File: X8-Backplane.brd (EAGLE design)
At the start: 122.1 x 106.6 mm, 14 parts, among them U1 LM2678

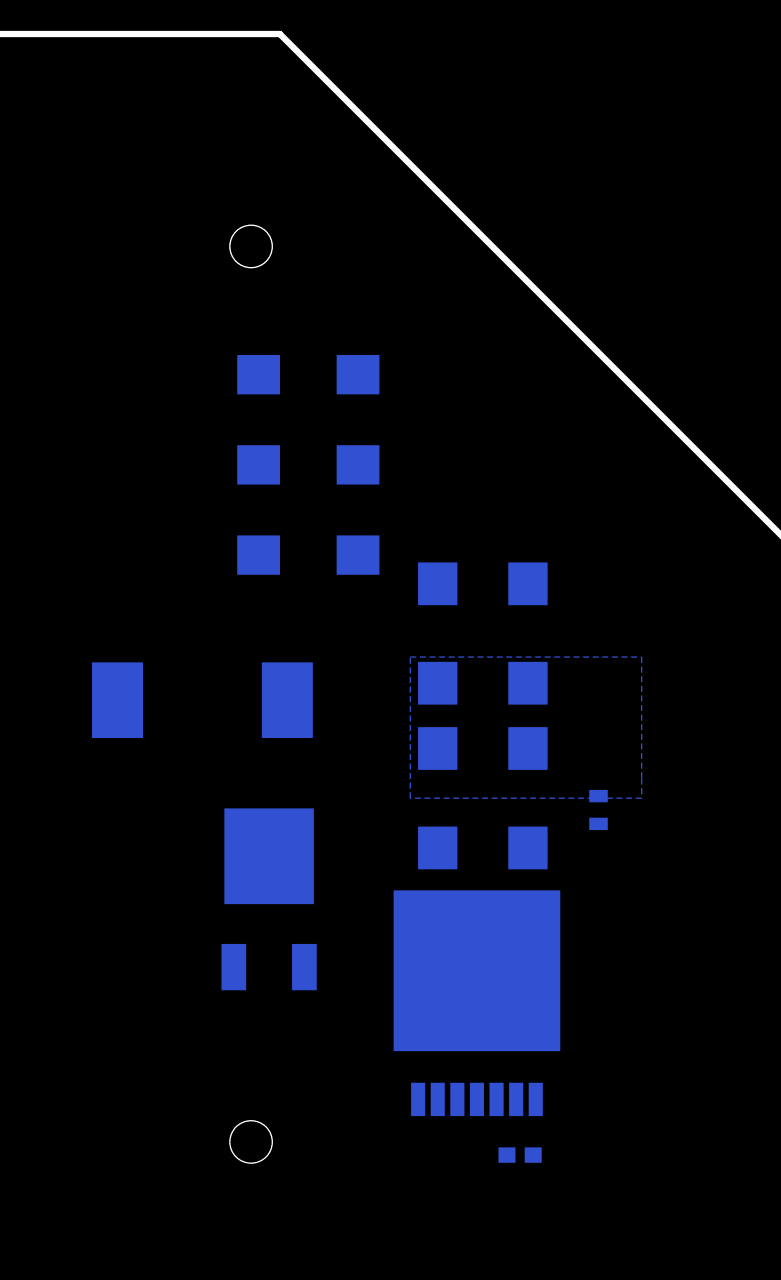
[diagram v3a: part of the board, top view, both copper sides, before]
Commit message: Finished preliminary layout - probably needs revision
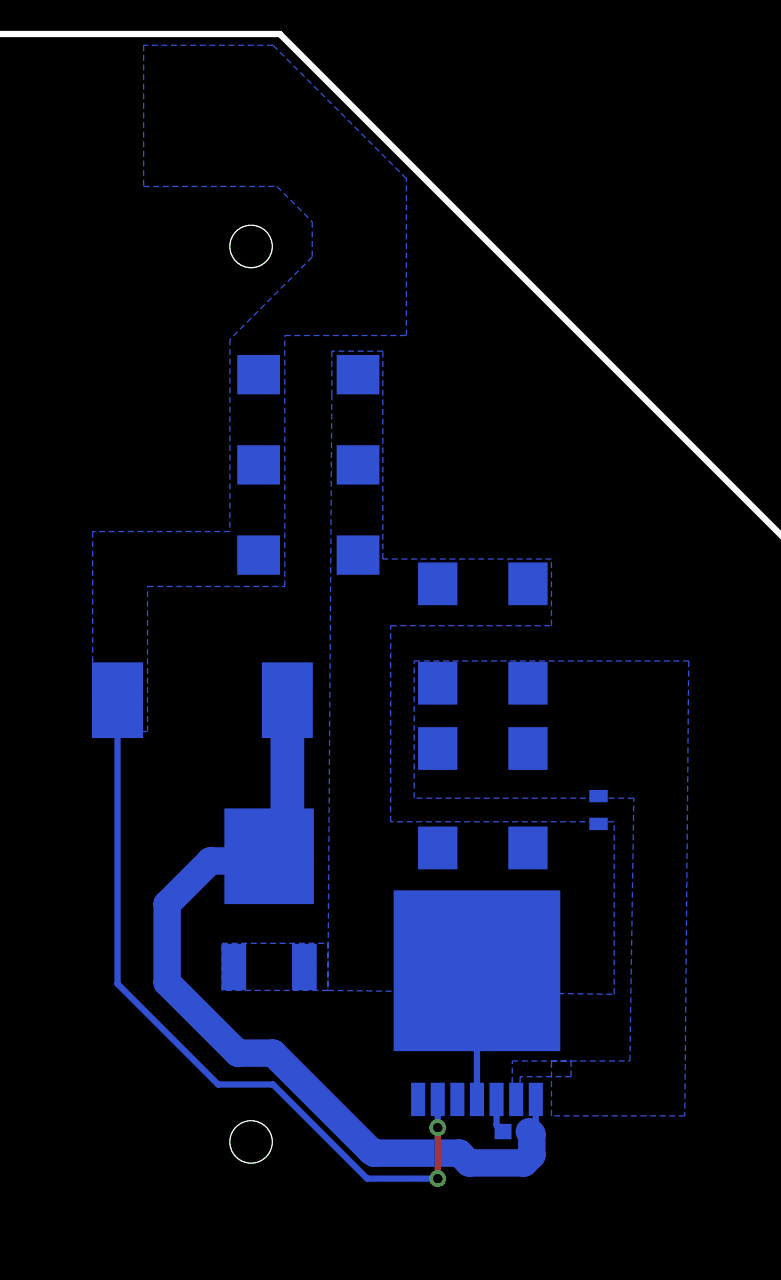
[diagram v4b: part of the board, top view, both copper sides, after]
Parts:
- moved C4 1.55 mm to (103.9, 28.2)
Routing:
- net N$3: track 0.00 -> 56.7 mm
- net +5V: track 0.00 -> 49.5 mm, vias 0 -> 2
- net GND: track 0.00 -> 8.33 mm
- net N$2: track 0.00 -> 2.26 mm
- added copper zone on layer 16, net +5V
- added copper zone on layer 16, net GND
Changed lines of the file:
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@@
 <setting verticaltext="up"/>
 </settings>
-<grid distance="0.01" unitdist="inch" unit="inch" style="lines" multiple="1" display="yes" altdistance="0.025" altunitdist="inch" altunit="inch"/>
+<grid distance="0.01" unitdist="inch" unit="inch" style="lines" multiple="1" display="yes" altdistance="0.001" altunitdist="inch" altunit="inch"/>
 <layers>
 <layer number="1" name="Top" color="4" fill="1" visible="yes" active="yes"/>
@@
 <element name="U1" library="PowerComponents" package="LM2678" value="LM2678" x="101.346" y="38.608" rot="MR270"/>
 <element name="C3" library="SparkFun-Capacitors" package="0805" value="0.47uF" x="109.22" y="49.022" rot="MR270"/>
-<element name="C4" library="SparkFun-Passives" package="0603-CAP" value="0.01uF" x="104.14" y="26.67" rot="MR180"/>
+<element name="C4" library="SparkFun-Passives" package="0603-CAP" value="0.01uF" x="103.886" y="28.194" rot="MR180"/>
 <element name="U$2" library="DiscreteComponents" package="HCMA1305" value="15uH" x="83.566" y="56.134" rot="MR90"/>
 <element name="C6" library="PowerComponents" package="CTAN(7.30_4.30MM)" value="150uF" x="90.424" y="77.216" rot="MR180"/>
@@
 <contactref element="U1" pad="3"/>
 <contactref element="C4" pad="1"/>
-<wire x1="103.29" y1="26.67" x2="102.616" y2="30.2768" width="0" layer="19" extent="16-16"/>
+<wire x1="102.616" y1="30.2768" x2="102.616" y2="28.614" width="0.4064" layer="16"/>
+<wire x1="102.616" y1="28.614" x2="103.036" y2="28.194" width="0.4064" layer="16"/>
 </signal>
 <signal name="N$3">
@@
 <contactref element="U$2" pad="P$1"/>
 <contactref element="U$1" pad="P$4"/>
-<wire x1="87.884" y1="46.026" x2="89.066" y2="56.134" width="0" layer="19" extent="16-16"/>
-<wire x1="105.156" y1="30.2768" x2="87.884" y2="46.026" width="0" layer="19" extent="16-16"/>
-<wire x1="104.99" y1="26.67" x2="105.156" y2="30.2768" width="0" layer="19" extent="16-16"/>
+<wire x1="89.066" y1="56.134" x2="89.066" y2="47.664" width="2.1844" layer="16"/>
+<wire x1="89.066" y1="47.664" x2="87.122" y2="45.72" width="2.1844" layer="16"/>
+<wire x1="105.156" y1="30.2768" x2="105.156" y2="28.614" width="0.4064" layer="16"/>
+<wire x1="105.156" y1="28.614" x2="104.736" y2="28.194" width="0.4064" layer="16"/>
+<wire x1="87.122" y1="45.72" x2="84.074" y2="45.72" width="1.778" layer="16"/>
+<wire x1="84.074" y1="45.72" x2="81.28" y2="42.926" width="1.778" layer="16"/>
+<wire x1="81.28" y1="42.926" x2="81.28" y2="37.846" width="1.778" layer="16"/>
+<wire x1="81.28" y1="37.846" x2="85.852" y2="33.274" width="1.778" layer="16"/>
+<wire x1="85.852" y1="33.274" x2="88.138" y2="33.274" width="1.778" layer="16"/>
+<wire x1="88.138" y1="33.274" x2="94.488" y2="26.924" width="1.778" layer="16"/>
+<wire x1="94.488" y1="26.924" x2="94.5642" y2="26.924" width="1.778" layer="16"/>
+<wire x1="94.5642" y1="26.924" x2="94.6912" y2="26.797" width="1.778" layer="16"/>
+<wire x1="94.6912" y1="26.797" x2="100.203" y2="26.797" width="1.778" layer="16"/>
+<wire x1="100.203" y1="26.797" x2="100.838" y2="26.162" width="1.778" layer="16"/>
+<wire x1="100.838" y1="26.162" x2="104.394" y2="26.162" width="1.778" layer="16"/>
+<wire x1="104.394" y1="26.162" x2="104.902" y2="26.67" width="1.778" layer="16"/>
+<wire x1="104.902" y1="26.67" x2="104.902" y2="28.028" width="1.778" layer="16"/>
+<wire x1="104.902" y1="28.028" x2="104.736" y2="28.194" width="1.778" layer="16"/>
+<wire x1="87.122" y1="45.72" x2="87.578" y2="45.72" width="1.778" layer="16"/>
+<wire x1="87.578" y1="45.72" x2="87.884" y2="46.026" width="1.778" layer="16"/>
 </signal>
 <signal name="GND">
@@
 <contactref element="C2" pad="-"/>
 <contactref element="C12" pad="-"/>
-<wire x1="98.806" y1="63.672" x2="104.648" y2="63.672" width="0" layer="19" extent="16-16"/>
-<wire x1="93.644" y1="65.532" x2="98.806" y2="63.672" width="0" layer="19" extent="16-16"/>
-<wire x1="93.644" y1="71.374" x2="93.644" y2="65.532" width="0" layer="19" extent="16-16"/>
-<wire x1="93.644" y1="77.216" x2="93.644" y2="71.374" width="0" layer="19" extent="16-16"/>
-<wire x1="109.22" y1="48.122" x2="104.648" y2="63.672" width="0" layer="19" extent="16-16"/>
-<wire x1="104.648" y1="46.564" x2="109.22" y2="48.122" width="0" layer="19" extent="16-16"/>
-<wire x1="98.806" y1="46.564" x2="104.648" y2="46.564" width="0" layer="19" extent="16-16"/>
-<wire x1="101.346" y1="38.608" x2="98.806" y2="46.564" width="0" layer="19" extent="16-16"/>
-<wire x1="90.169" y1="38.846" x2="101.346" y2="38.608" width="0" layer="19" extent="16-16"/>
-<wire x1="85.599" y1="38.846" x2="90.169" y2="38.846" width="0" layer="19" extent="16-16"/>
-<wire x1="101.346" y1="30.2768" x2="101.346" y2="38.608" width="0" layer="19" extent="16-16"/>
+<polygon width="0.4064" layer="16">
+<vertex x="95.25" y="78.74"/>
+<vertex x="91.948" y="78.74"/>
+<vertex x="91.948" y="75.946"/>
+<vertex x="91.694" y="37.338"/>
+<vertex x="110.236" y="37.084"/>
+<vertex x="110.236" y="48.26"/>
+<vertex x="95.758" y="48.26"/>
+<vertex x="95.758" y="60.96"/>
+<vertex x="106.172" y="60.96"/>
+<vertex x="106.172" y="65.278"/>
+<vertex x="95.25" y="65.278"/>
+</polygon>
+<wire x1="101.346" y1="30.2768" x2="101.346" y2="38.608" width="0.4064" layer="16"/>
+<polygon width="0.4064" layer="16">
+<vertex x="84.836" y="40.386"/>
+<vertex x="91.694" y="40.386"/>
+<vertex x="91.694" y="37.338"/>
+<vertex x="84.836" y="37.338"/>
+</polygon>
 </signal>
 <signal name="+12V">
@@
 <contactref element="C12" pad="+"/>
 <polygon width="0.4064" layer="16">
-<vertex x="97.028" y="58.928"/>
-<vertex x="112.014" y="58.928"/>
-<vertex x="112.014" y="51.054"/>
-<vertex x="112.014" y="49.784"/>
-<vertex x="97.028" y="49.784"/>
+<vertex x="97.282" y="58.674"/>
+<vertex x="115.062" y="58.674"/>
+<vertex x="114.808" y="29.21"/>
+<vertex x="106.172" y="29.21"/>
+<vertex x="106.172" y="32.766"/>
+<vertex x="111.252" y="32.766"/>
+<vertex x="111.506" y="49.784"/>
+<vertex x="97.282" y="49.784"/>
 </polygon>
-<wire x1="109.22" y1="49.922" x2="103.886" y2="30.2768" width="0" layer="19" extent="16-16"/>
+<polygon width="0.4064" layer="16">
+<vertex x="103.632" y="29.464"/>
+<vertex x="103.632" y="32.766"/>
+<vertex x="107.442" y="32.766"/>
+<vertex x="107.442" y="31.75"/>
+<vertex x="104.14" y="31.75"/>
+<vertex x="104.14" y="29.464"/>
+</polygon>
 </signal>
 <signal name="+5V">
@@
 <contactref element="C9" pad="+"/>
 <contactref element="C10" pad="+"/>
-<wire x1="87.204" y1="71.374" x2="87.204" y2="77.216" width="0" layer="19" extent="16-16"/>
-<wire x1="87.204" y1="65.532" x2="87.204" y2="71.374" width="0" layer="19" extent="16-16"/>
-<wire x1="78.066" y1="56.134" x2="87.204" y2="65.532" width="0" layer="19" extent="16-16"/>
-<wire x1="98.806" y1="30.2768" x2="78.066" y2="56.134" width="0" layer="19" extent="16-16"/>
+<polygon width="0.4064" layer="16">
+<vertex x="76.454" y="54.102"/>
+<vertex x="80.01" y="54.102"/>
+<vertex x="80.01" y="63.5"/>
+<vertex x="88.9" y="63.5"/>
+<vertex x="88.9" y="79.756"/>
+<vertex x="96.774" y="79.756"/>
+<vertex x="96.774" y="89.916"/>
+<vertex x="88.138" y="98.552"/>
+<vertex x="79.756" y="98.552"/>
+<vertex x="79.756" y="89.408"/>
+<vertex x="88.392" y="89.408"/>
+<vertex x="90.678" y="87.122"/>
+<vertex x="90.678" y="84.836"/>
+<vertex x="85.344" y="79.502"/>
+<vertex x="85.344" y="67.056"/>
+<vertex x="76.454" y="67.056"/>
+</polygon>
+<wire x1="78.066" y1="56.134" x2="78.066" y2="37.758" width="0.4064" layer="16"/>
+<wire x1="78.066" y1="37.758" x2="84.582" y2="31.242" width="0.4064" layer="16"/>
+<wire x1="84.582" y1="31.242" x2="88.138" y2="31.242" width="0.4064" layer="16"/>
+<wire x1="88.138" y1="31.242" x2="94.234" y2="25.146" width="0.4064" layer="16"/>
+<wire x1="94.234" y1="25.146" x2="98.806" y2="25.146" width="0.4064" layer="16"/>
+<via x="98.806" y="25.146" extent="1-16" drill="0.6"/>
+<wire x1="98.806" y1="25.146" x2="98.806" y2="28.448" width="0.4064" layer="1"/>
+<via x="98.806" y="28.448" extent="1-16" drill="0.6"/>
+<wire x1="98.806" y1="28.448" x2="98.806" y2="30.2768" width="0.4064" layer="16"/>
 </signal>
 <signal name="N$4">

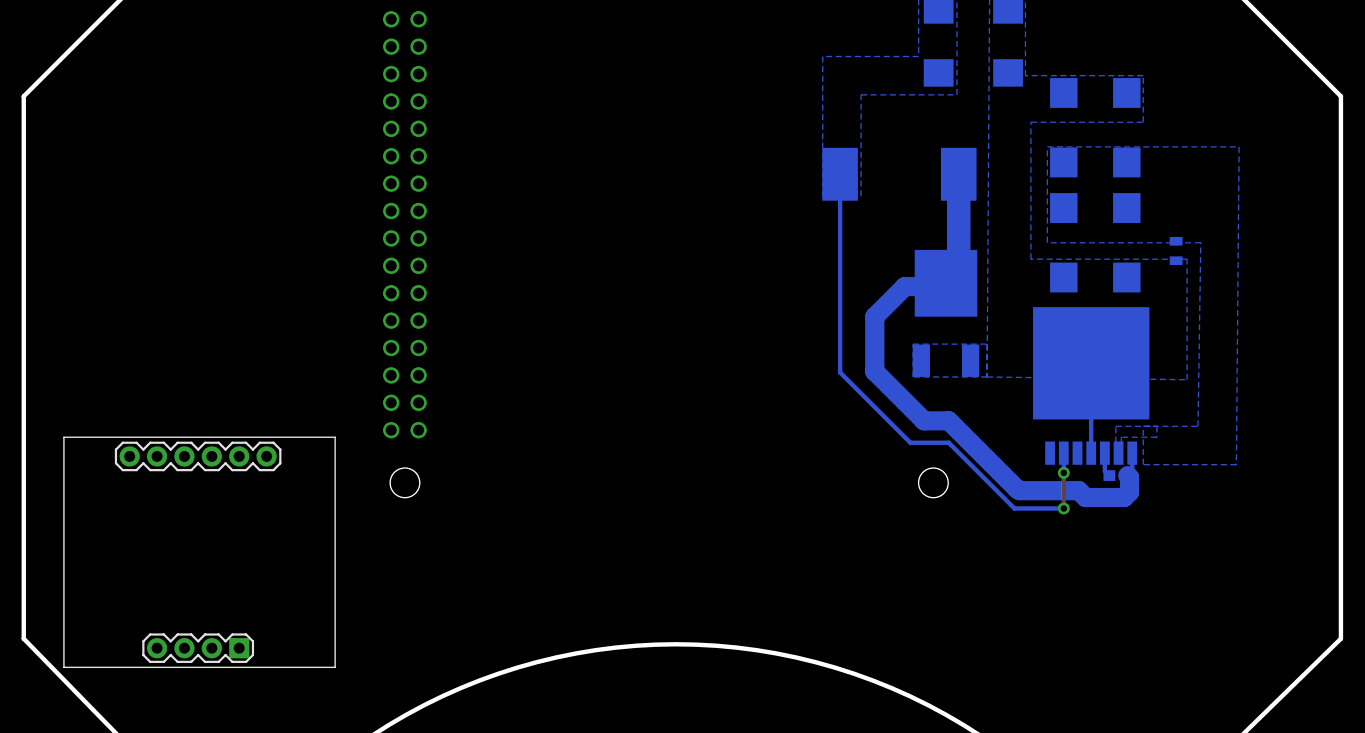
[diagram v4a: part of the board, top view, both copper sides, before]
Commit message: added brd to brd connector
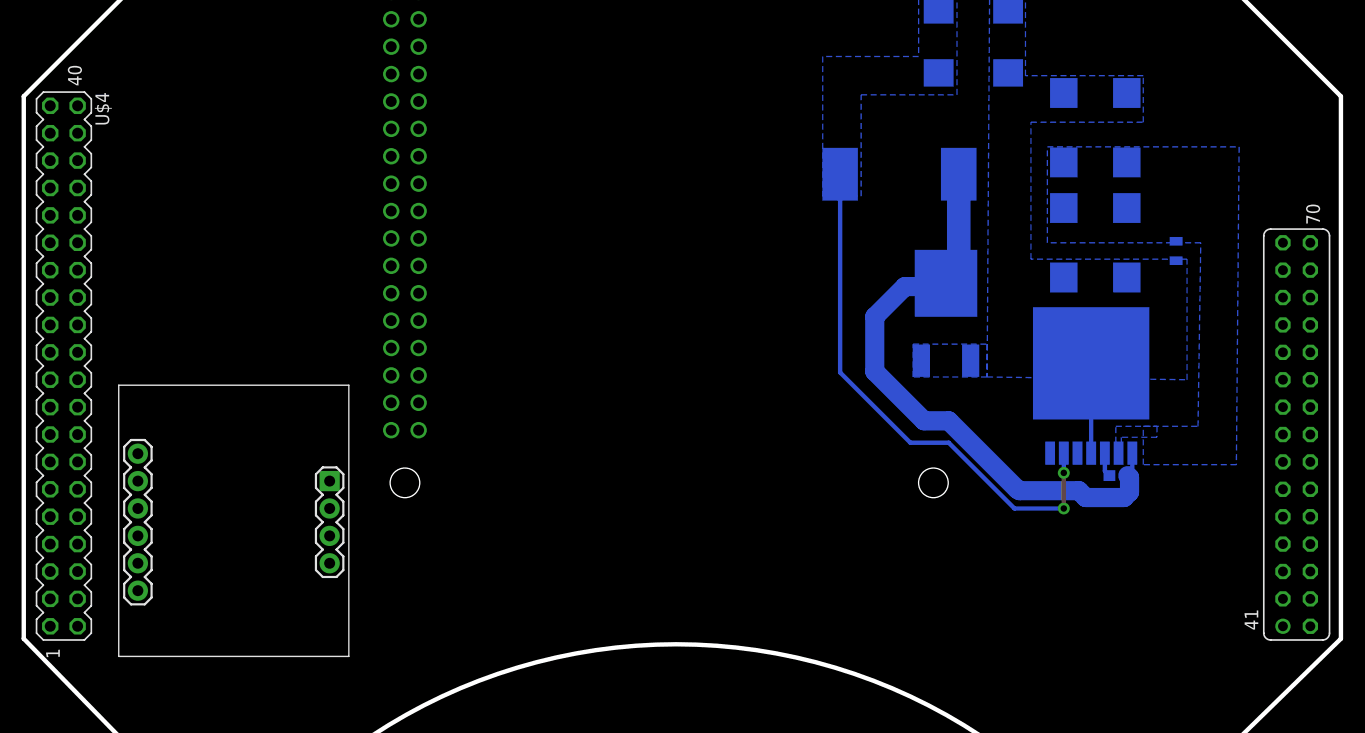
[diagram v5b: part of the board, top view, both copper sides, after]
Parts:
- added U$4: SHIELDCONNECTOR, backplane_to_shield_connector:MA20-2
- moved U$3 4.54 mm to (21.8, 25.1), turned to 0 degrees
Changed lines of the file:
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@@
 <element name="C13" library="PowerComponents" package="CTAN(7.30_4.30MM)" value="10uF" x="104.648" y="49.784" rot="MR270"/>
 <element name="C2" library="PowerComponents" package="CTAN(7.30_4.30MM)" value="10uF" x="104.648" y="60.452" rot="MR90"/>
-<element name="U$3" library="Other" package="BNO055" value="BNO055_9DOF_BREAKOUT" x="19.812" y="21.082" rot="R270"/>
+<element name="U$3" library="Other" package="BNO055" value="BNO055_9DOF_BREAKOUT" x="21.844" y="25.146"/>
+<element name="U$4" library="backplane_to_shield_connector" package="MA20-2" value="SHIELDCONNECTOR" x="60.706" y="40.894"/>
 </elements>
 <signals>
@@
 <vertex x="84.836" y="37.338"/>
 </polygon>
+<wire x1="93.644" y1="71.374" x2="93.644" y2="77.216" width="0" layer="19" extent="16-16"/>
+<wire x1="93.644" y1="65.532" x2="93.644" y2="71.374" width="0" layer="19" extent="16-16"/>
+<wire x1="98.806" y1="63.672" x2="93.644" y2="65.532" width="0" layer="19" extent="16-16"/>
+<wire x1="104.648" y1="63.672" x2="98.806" y2="63.672" width="0" layer="19" extent="16-16"/>
+<wire x1="109.22" y1="48.122" x2="104.648" y2="63.672" width="0" layer="19" extent="16-16"/>
+<wire x1="104.648" y1="46.564" x2="109.22" y2="48.122" width="0" layer="19" extent="16-16"/>
+<wire x1="98.806" y1="46.564" x2="104.648" y2="46.564" width="0" layer="19" extent="16-16"/>
+<wire x1="101.346" y1="38.608" x2="98.806" y2="46.564" width="0" layer="19" extent="16-16"/>
+<wire x1="90.169" y1="38.846" x2="101.346" y2="38.608" width="0" layer="19" extent="16-16"/>
+<wire x1="85.599" y1="38.846" x2="90.169" y2="38.846" width="0" layer="19" extent="16-16"/>
 </signal>
 <signal name="+12V">

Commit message: because I can
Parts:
- added IC1: MAX3467CPA, maxim:SO08
- added U$7: PCA9615, test_lib:MSOP_10
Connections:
- new net +3V3: IC1.1
- new net COM_A: IC1.8
- new net COM_B: IC1.7
- new net COM_Y: IC1.5
- new net COM_Z: IC1.6
- new net TETHER_RX: IC1.2
- new net TETHER_TX: IC1.3
- net GND: now also IC1.4
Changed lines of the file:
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@@
 <setting verticaltext="up"/>
 </settings>
-<grid distance="0.01" unitdist="inch" unit="inch" style="lines" multiple="1" display="yes" altdistance="0.001" altunitdist="inch" altunit="inch"/>
+<grid distance="1" unitdist="mil" unit="mil" style="lines" multiple="1" display="yes" altdistance="0.001" altunitdist="inch" altunit="inch"/>
 <layers>
 <layer number="1" name="Top" color="4" fill="1" visible="yes" active="yes"/>
@@
 <element name="U$3" library="Other" package="BNO055" value="BNO055_9DOF_BREAKOUT" x="21.844" y="25.146"/>
 <element name="U$4" library="backplane_to_shield_connector" package="MA20-2" value="SHIELDCONNECTOR" x="60.706" y="40.894"/>
+<element name="IC1" library="maxim" package="SO08" value="MAX3467CPA" x="-5.1562" y="-45.0088">
+<attribute name="OC_NEWARK" value="unknown" x="-14.2494" y="-28.6258" size="1.778" layer="27" display="off"/>
+<attribute name="MPN" value="" x="-14.2494" y="-28.6258" size="1.778" layer="27" display="off"/>
+<attribute name="OC_FARNELL" value="unknown" x="-14.2494" y="-28.6258" size="1.778" layer="27" display="off"/>
+<attribute name="MF" value="" x="-14.2494" y="-28.6258" size="1.778" layer="27" display="off"/>
+</element>
+<element name="U$7" library="test_lib" package="MSOP_10" value="PCA9615" x="-7.9248" y="-54.991"/>
 </elements>
 <signals>
@@
 <vertex x="84.836" y="37.338"/>
 </polygon>
+<contactref element="IC1" pad="4"/>
 <wire x1="93.644" y1="71.374" x2="93.644" y2="77.216" width="0" layer="19" extent="16-16"/>
 <wire x1="93.644" y1="65.532" x2="93.644" y2="71.374" width="0" layer="19" extent="16-16"/>
@@
 <wire x1="90.169" y1="38.846" x2="101.346" y2="38.608" width="0" layer="19" extent="16-16"/>
 <wire x1="85.599" y1="38.846" x2="90.169" y2="38.846" width="0" layer="19" extent="16-16"/>
+<wire x1="-3.2512" y1="-48.0822" x2="85.599" y2="38.846" width="0" layer="19" extent="1-16"/>
 </signal>
 <signal name="+12V">
@@
 <via x="98.806" y="28.448" extent="1-16" drill="0.6"/>
 <wire x1="98.806" y1="28.448" x2="98.806" y2="30.2768" width="0.4064" layer="16"/>
+<wire x1="87.204" y1="71.374" x2="87.204" y2="77.216" width="0" layer="19" extent="16-16"/>
+<wire x1="87.204" y1="65.532" x2="87.204" y2="71.374" width="0" layer="19" extent="16-16"/>
+<wire x1="78.066" y1="56.134" x2="87.204" y2="65.532" width="0" layer="19" extent="16-16"/>
 </signal>
 <signal name="N$4">
 <contactref element="PCB1" pad="P$1"/>
 </signal>
+<signal name="+3V3">
+<contactref element="IC1" pad="1"/>
+</signal>
+<signal name="TETHER_RX">
+<contactref element="IC1" pad="2"/>
+</signal>
+<signal name="TETHER_TX">
+<contactref element="IC1" pad="3"/>
+</signal>
+<signal name="COM_A">
+<contactref element="IC1" pad="8"/>
+</signal>
+<signal name="COM_B">
+<contactref element="IC1" pad="7"/>
+</signal>
+<signal name="COM_Y">
+<contactref element="IC1" pad="5"/>
+</signal>
+<signal name="COM_Z">
+<contactref element="IC1" pad="6"/>
+</signal>
 </signals>
